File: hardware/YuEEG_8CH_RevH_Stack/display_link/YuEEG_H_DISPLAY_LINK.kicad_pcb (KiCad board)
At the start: 2 copper layers, 8.3 x 13.6 mm, 2 parts

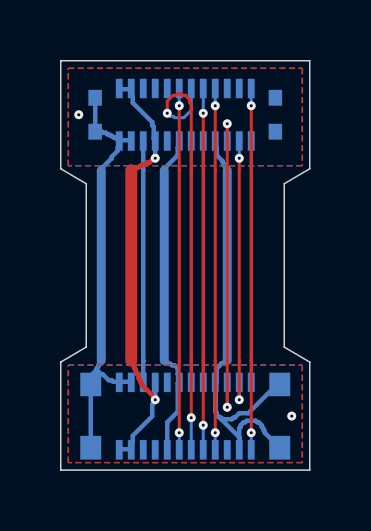
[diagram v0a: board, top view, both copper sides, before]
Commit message: Narrow display FPC fold to clear neighboring digital components
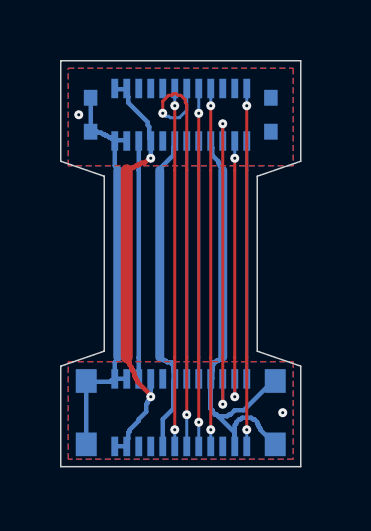
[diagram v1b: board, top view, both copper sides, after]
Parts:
- moved JF2 0.19 mm to (4.00, 11.7)
- moved JF1 0.15 mm to (4.00, 1.80)
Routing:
- net GND: track 44.1 -> 43.5 mm
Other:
- board size 8.3 x 13.6 mm -> 8 x 13.5 mm
